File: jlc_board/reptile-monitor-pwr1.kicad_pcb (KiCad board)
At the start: 4 copper layers, 38.1 x 38 mm, 39 parts, among them J1 1-WIRE, J2 UART, J3 Conn_01x04, J6 I/O, J8 I2C, SW1 RESET, SW2 BOOT, U1 AP2112M-3.3

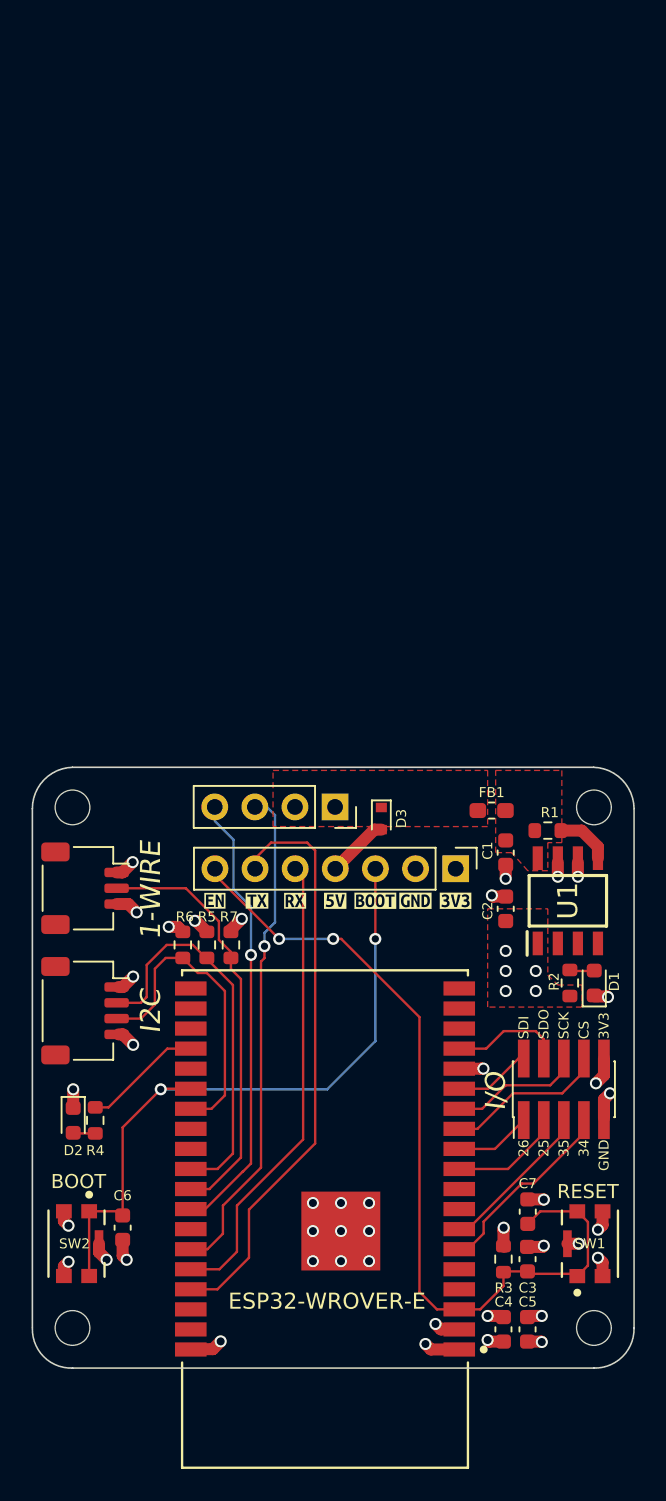
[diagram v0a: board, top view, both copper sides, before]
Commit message: separate power board
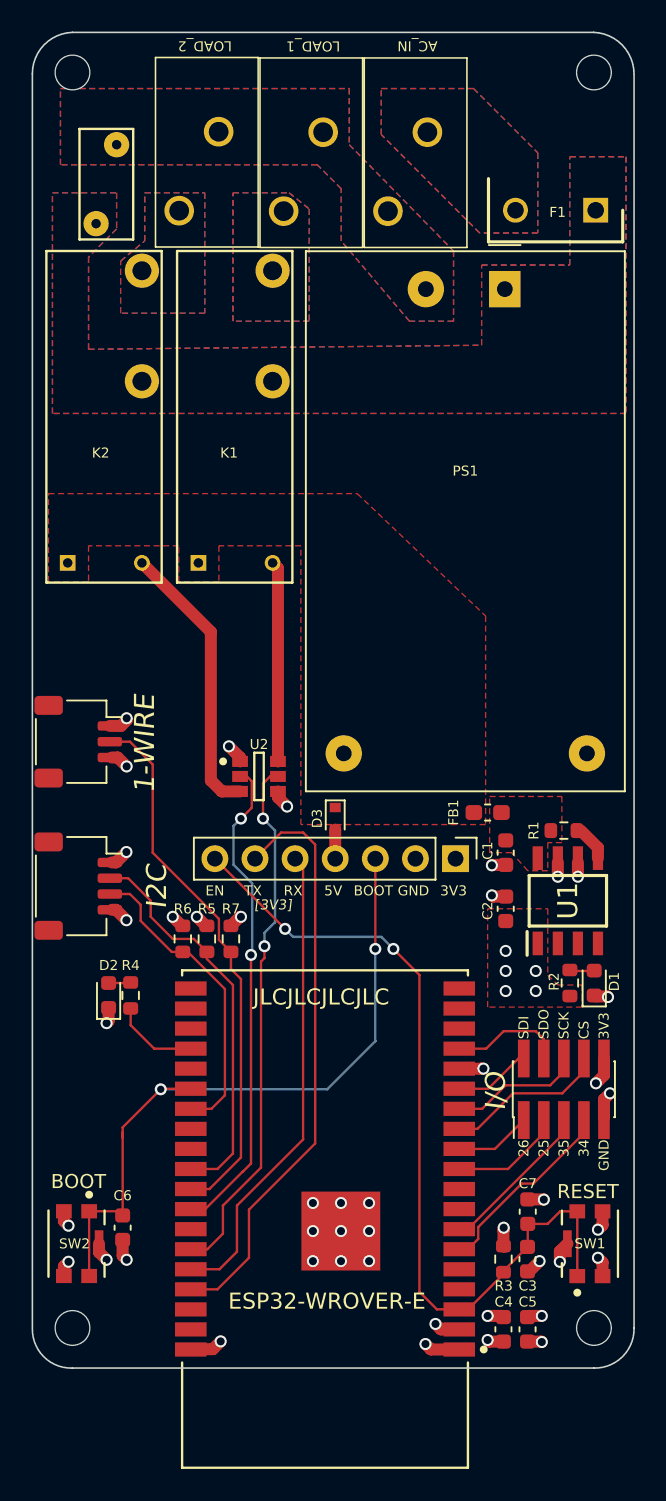
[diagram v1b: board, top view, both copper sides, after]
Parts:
- removed the svg2mod at (113.2, 105.8)
- removed the svg2mod at (128.4, 105.8)
- removed the svg2mod at (123.3, 105.8)
- removed the svg2mod at (115.8, 105.8)
- removed the svg2mod at (118.2, 105.8)
- removed the svg2mod at (125.9, 105.8)
- removed the svg2mod at (120.8, 105.8)
- added F1: 39208000440, SamacSys_Parts:TO508P400X850X850-2P, F.Cu at (137.3, 62.1)
- added J4: LOAD_1, SamacSys_Parts:128340212, F.Cu at (120.0, 57.1)
- added J5: LOAD_2, SamacSys_Parts:128340212, F.Cu at (113.4, 57.1)
- added K1: ALDP105W, reptile-monitor:Panasonic-ALDP105W-Manufacturer_Recommended, F.Cu at (112.1, 84.4)
- added K2: ALDP105W, reptile-monitor:Panasonic-ALDP105W-Manufacturer_Recommended, F.Cu at (103.8, 84.4)
- added PS1: HLK-PM01, Converter_ACDC:Converter_ACDC_HiLink_HLK-PMxx, F.Cu at (131.5, 67.1)
- added RV1: Varistor, Varistor:RV_Disc_D7mm_W3.4mm_P5mm, F.Cu at (106.9, 57.9)
- added U2: NUD3105DMT1G, reptile-monitor:ON_Semi-318F-0-0-0, F.Cu at (116.0, 97.9)
- added svg2mod: G***, svg2mod, B.Cu at (132.1, 91.2)
- J3: value Conn_01x04 -> AC_IN; footprint Connector_PinSocket_2.54mm:PinSocket_1x04_P2.54mm_Vertical -> SamacSys_Parts:128340212
- moved REF1 46.5 mm to (137.2, 53.3)
- moved REF1 46.5 mm to (104.1, 53.3)
- moved J3 43.1 mm to (126.6, 57.1), turned to 180 degrees
- moved J1 9.29 mm to (104.5, 95.7)
- moved D2 8.22 mm to (106.4, 111.8), turned to 90 degrees
- moved R4 8.22 mm to (107.8, 111.8), turned to -90 degrees
- moved J8 7.90 mm to (104.5, 104.9)
- moved D3 2.92 mm to (120.8, 100.6)
- moved R1 1.02 mm to (135.3, 101.3)
- moved J2 0.64 mm to (128.4, 103.1)
- moved R5 0.38 mm to (112.6, 108.2)
- moved R6 0.38 mm to (111.1, 108.2)
- moved R7 0.38 mm to (114.2, 108.2)
- moved FB1 0.28 mm to (130.4, 100.2)
- turned C3 to -90 degrees
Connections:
- net EN renamed /EN
- J3 pad 1: GND -> /AC_L
- J3 pad 2: +5V -> /AC_N
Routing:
- net /RLY2: track 0.00 -> 17.7 mm
- net /RLY1: track 0.00 -> 12.7 mm
- net 1-WIRE: track 26.9 -> 34.5 mm
- net L1: track 26.7 -> 31.1 mm, vias 1 -> 2
- net GND: track 27.9 -> 30.8 mm, vias 32 -> 34
- net /LED: track 7.59 -> 5.48 mm
- net Net-(D3-Pad2): track 3.94 -> 1.84 mm
- net L2: track 32.1 -> 33.8 mm, vias 1 -> 2
- net /PWR_EN: track 3.49 -> 2.19 mm
- net +3V3: track 12.6 -> 11.6 mm
- net TXD0: track 36.5 -> 37.2 mm
- net RXD0: track 29.5 -> 30.2 mm
- added copper zone on B.Cu, net /AC_L
- added copper zone on F.Cu, net /AC_L
- added copper zone on In1.Cu, net /AC_L
- added copper zone on In2.Cu, net /AC_L
- added copper zone on B.Cu, net /AC_N
- added copper zone on F.Cu, net /AC_N
- added copper zone on In1.Cu, net /AC_N
- added copper zone on In2.Cu, net /AC_N
- added copper zone on B.Cu, net /FUSED_AC_L
- added copper zone on F.Cu, net /FUSED_AC_L
- added copper zone on In1.Cu, net /FUSED_AC_L
- added copper zone on In2.Cu, net /FUSED_AC_L
- added copper zone on B.Cu, net /LOAD1
- added copper zone on F.Cu, net /LOAD1
- added copper zone on In1.Cu, net /LOAD1
- added copper zone on In2.Cu, net /LOAD1
- added copper zone on B.Cu, net /LOAD2
- added copper zone on F.Cu, net /LOAD2
- added copper zone on In1.Cu, net /LOAD2
- added copper zone on In2.Cu, net /LOAD2
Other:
- board size 38.1 x 38 mm -> 38.1 x 84.6 mm
- board text added: "5V"
- board text added: "BOOT"
- board text added: "EN"
- board text added: "Mike Pleimann"
- board text added: "RX"
- board text added: "Rev. 3 June 2021"
- board text added: "TX"
- board text added: "[3V3]"
- board text removed: "Rev. 3 July 2021"
